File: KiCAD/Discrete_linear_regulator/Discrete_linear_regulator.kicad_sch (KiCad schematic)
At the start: 40 parts, among them J1 Conn_01x06, Q1 PZT2222AT3G, Q10 BC857, Q11 BC857, Q2 BC857, Q3 BC857, Q4 PZT2222AT3G, Q5 PZT2907AT3G, Q8 PZT2907AT3G, U1 LM4562

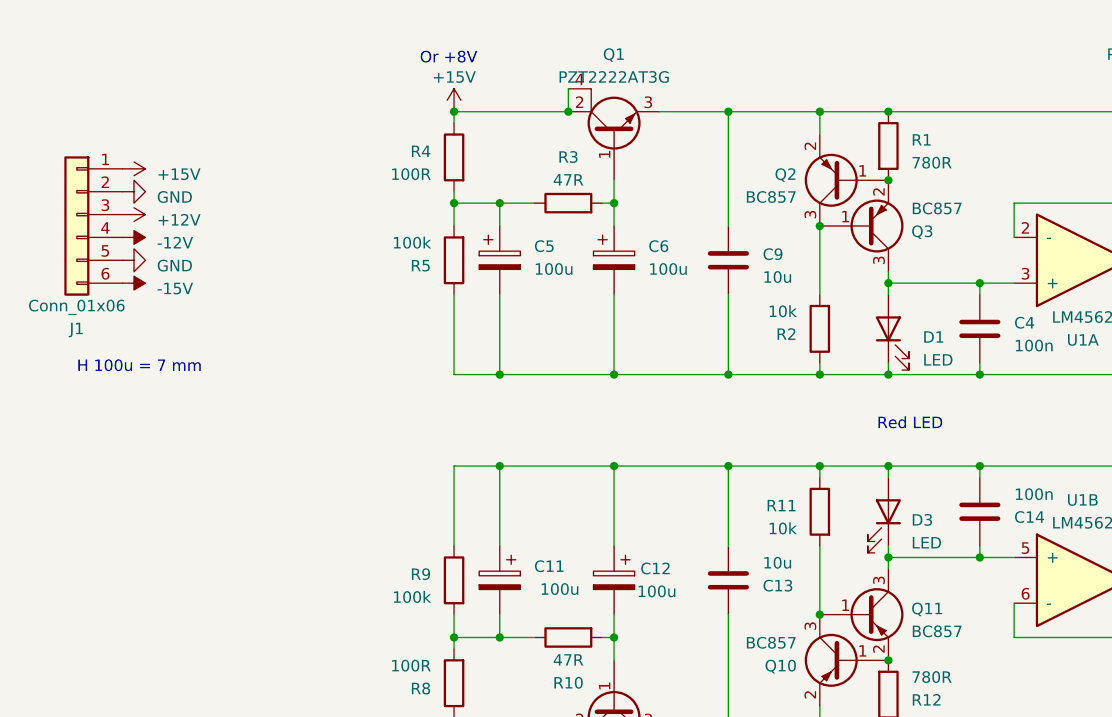
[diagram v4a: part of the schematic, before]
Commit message: linear regulators changes
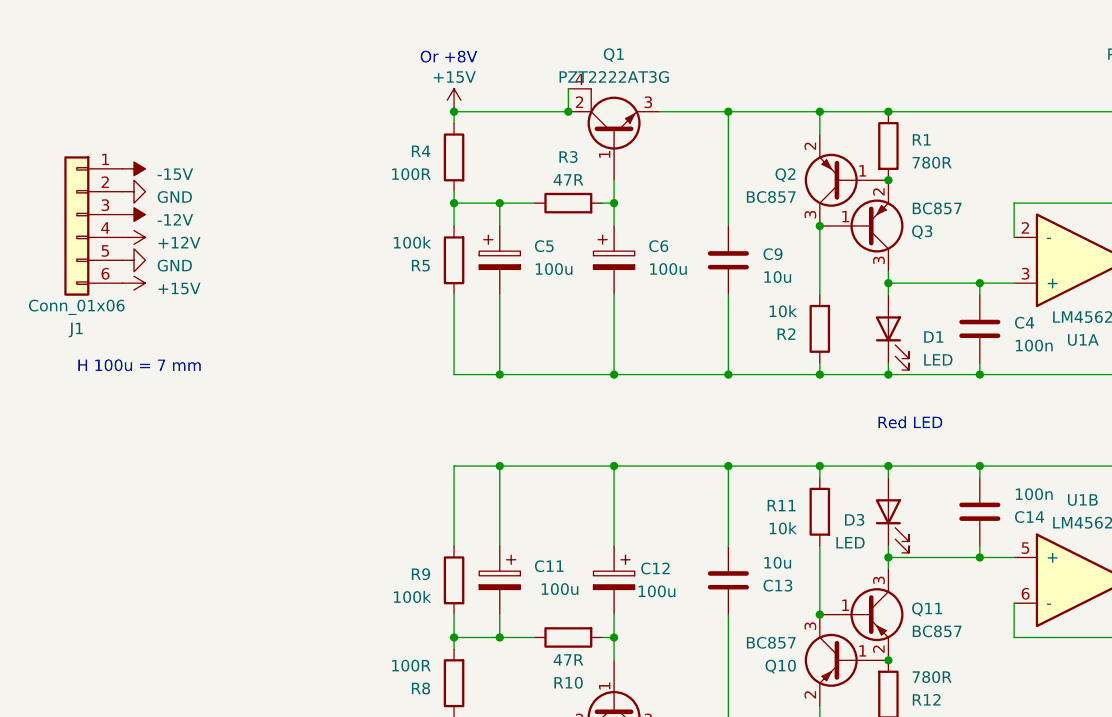
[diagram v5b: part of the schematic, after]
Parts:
- D1, D3: footprint (none) -> LED_SMD:LED_0805_2012Metric
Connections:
- net +12V: now also J1.4 (Pin_4); no longer J1.3 (Pin_3)
- net +15V: now also J1.6 (Pin_6); no longer J1.1 (Pin_1)
- net -12V: now also J1.3 (Pin_3); no longer J1.4 (Pin_4)
- net -15V: now also J1.1 (Pin_1); no longer J1.6 (Pin_6)
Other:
- moved on the sheet: D3
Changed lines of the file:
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@@
       (effects (font (size 1.27 1.27) italic) (justify left) hide)
     )
-    (property "Datasheet" "https://www.onsemi.com/pub/Collateral/BC860-D.pdf" (at 105.41 120.65 0)
+    (property "Datasheet" "" (at 105.41 120.65 0)
       (effects (font (size 1.27 1.27)) (justify left) hide)
     )
@@
     )
   )
+  (symbol (lib_id "power:-15V") (at 25.4 66.04 270) (unit 1)
+    (in_bom yes) (on_board yes) (dnp no) (fields_autoplaced)
+    (property "Reference" "#PWR013" (at 27.94 66.04 0)
+      (effects (font (size 1.27 1.27)) hide)
+    )
+    (property "Value" "-15V" (at 29.21 66.675 90)
+      (effects (font (size 1.27 1.27)) (justify left))
+    )
+    (property "Footprint" "" (at 25.4 66.04 0)
+      (effects (font (size 1.27 1.27)) hide)
+    )
+    (property "Datasheet" "" (at 25.4 66.04 0)
+      (effects (font (size 1.27 1.27)) hide)
+    )
+    (pin "1")
+    (instances
+      (project "Discrete_linear_regulator"
+        (path "/19504711-657f-4df2-b2e9-322b7e64e4f7"
+          (reference "#PWR013") (unit 1)
+        )
+      )
+    )
+  )
+  (symbol (lib_id "power:+15V") (at 25.4 78.74 270) (unit 1)
+    (in_bom yes) (on_board yes) (dnp no) (fields_autoplaced)
+    (property "Reference" "#PWR014" (at 21.59 78.74 0)
+      (effects (font (size 1.27 1.27)) hide)
+    )
+    (property "Value" "+15V" (at 29.21 79.375 90)
+      (effects (font (size 1.27 1.27)) (justify left))
+    )
+    (property "Footprint" "" (at 25.4 78.74 0)
+      (effects (font (size 1.27 1.27)) hide)
+    )
+    (property "Datasheet" "" (at 25.4 78.74 0)
+      (effects (font (size 1.27 1.27)) hide)
+    )
+    (pin "1")
+    (instances
+      (project "Discrete_linear_regulator"
+        (path "/19504711-657f-4df2-b2e9-322b7e64e4f7"
+          (reference "#PWR014") (unit 1)
+        )
+      )
+    )
+  )
   (symbol (lib_id "Audio_DSP:PZT2222AT3G") (at 80.01 60.96 90) (unit 1)
     (in_bom yes) (on_board yes) (dnp no) (fields_autoplaced)
@@
         (path "/19504711-657f-4df2-b2e9-322b7e64e4f7"
           (reference "C11") (unit 1)
-        )
-      )
-    )
-  )
-  (symbol (lib_id "power:+12V") (at 25.4 71.12 270) (unit 1)
-    (in_bom yes) (on_board yes) (dnp no) (fields_autoplaced)
-    (property "Reference" "#PWR09" (at 21.59 71.12 0)
-      (effects (font (size 1.27 1.27)) hide)
-    )
-    (property "Value" "+12V" (at 29.21 71.755 90)
-      (effects (font (size 1.27 1.27)) (justify left))
-    )
-    (property "Footprint" "" (at 25.4 71.12 0)
-      (effects (font (size 1.27 1.27)) hide)
-    )
-    (property "Datasheet" "" (at 25.4 71.12 0)
-      (effects (font (size 1.27 1.27)) hide)
-    )
-    (pin "1")
-    (instances
-      (project "Discrete_linear_regulator"
-        (path "/19504711-657f-4df2-b2e9-322b7e64e4f7"
-          (reference "#PWR09") (unit 1)
         )
       )
@@
       (effects (font (size 1.27 1.27) italic) (justify left) hide)
     )
-    (property "Datasheet" "https://www.onsemi.com/pub/Collateral/BC860-D.pdf" (at 107.95 72.39 0)
+    (property "Datasheet" "" (at 107.95 72.39 0)
       (effects (font (size 1.27 1.27)) (justify left) hide)
     )
@@
     )
   )
-  (symbol (lib_id "Device:LED") (at 110.49 104.14 270) (mirror x) (unit 1)
-    (in_bom yes) (on_board yes) (dnp no) (fields_autoplaced)
-    (property "Reference" "D3" (at 113.03 105.0925 90)
-      (effects (font (size 1.27 1.27)) (justify left))
-    )
-    (property "Value" "LED" (at 113.03 107.6325 90)
-      (effects (font (size 1.27 1.27)) (justify left))
-    )
-    (property "Footprint" "" (at 110.49 104.14 0)
-      (effects (font (size 1.27 1.27)) hide)
-    )
-    (property "Datasheet" "~" (at 110.49 104.14 0)
+  (symbol (lib_id "Device:LED") (at 110.49 104.14 90) (unit 1)
+    (in_bom yes) (on_board yes) (dnp no)
+    (property "Reference" "D3" (at 107.95 105.0925 90)
+      (effects (font (size 1.27 1.27)) (justify left))
+    )
+    (property "Value" "LED" (at 107.95 107.6325 90)
+      (effects (font (size 1.27 1.27)) (justify left))
+    )
+    (property "Footprint" "LED_SMD:LED_0805_2012Metric" (at 110.49 104.14 0)
+      (effects (font (size 1.27 1.27)) hide)
+    )
+    (property "Datasheet" "https://nl.mouser.com/ProductDetail/Broadcom-Avago/HSMH-C170?qs=YDL0qNrpDT6b21G9HrN9ig%3D%3D" (at 110.49 104.14 0)
       (effects (font (size 1.27 1.27)) hide)
     )
@@
       (effects (font (size 1.27 1.27) italic) (justify left) hide)
     )
-    (property "Datasheet" "https://www.onsemi.com/pub/Collateral/BC860-D.pdf" (at 107.95 115.57 0)
+    (property "Datasheet" "" (at 107.95 115.57 0)
       (effects (font (size 1.27 1.27)) (justify left) hide)
     )
@@
         (path "/19504711-657f-4df2-b2e9-322b7e64e4f7"
           (reference "Q11") (unit 1)
-        )
-      )
-    )
-  )
-  (symbol (lib_id "power:-15V") (at 25.4 78.74 270) (unit 1)
-    (in_bom yes) (on_board yes) (dnp no) (fields_autoplaced)
-    (property "Reference" "#PWR08" (at 27.94 78.74 0)
-      (effects (font (size 1.27 1.27)) hide)
-    )
-    (property "Value" "-15V" (at 29.21 79.375 90)
-      (effects (font (size 1.27 1.27)) (justify left))
-    )
-    (property "Footprint" "" (at 25.4 78.74 0)
-      (effects (font (size 1.27 1.27)) hide)
-    )
-    (property "Datasheet" "" (at 25.4 78.74 0)
-      (effects (font (size 1.27 1.27)) hide)
-    )
-    (pin "1")
-    (instances
-      (project "Discrete_linear_regulator"
-        (path "/19504711-657f-4df2-b2e9-322b7e64e4f7"
-          (reference "#PWR08") (unit 1)
         )
       )
@@
     )
   )
-  (symbol (lib_id "power:+15V") (at 25.4 66.04 270) (unit 1)
-    (in_bom yes) (on_board yes) (dnp no) (fields_autoplaced)
-    (property "Reference" "#PWR07" (at 21.59 66.04 0)
-      (effects (font (size 1.27 1.27)) hide)
-    )
-    (property "Value" "+15V" (at 29.21 66.675 90)
-      (effects (font (size 1.27 1.27)) (justify left))
-    )
-    (property "Footprint" "" (at 25.4 66.04 0)
-      (effects (font (size 1.27 1.27)) hide)
-    )
-    (property "Datasheet" "" (at 25.4 66.04 0)
-      (effects (font (size 1.27 1.27)) hide)
-    )
-    (pin "1")
-    (instances
-      (project "Discrete_linear_regulator"
-        (path "/19504711-657f-4df2-b2e9-322b7e64e4f7"
-          (reference "#PWR07") (unit 1)
-        )
-      )
-    )
-  )
   (symbol (lib_id "power:GND") (at 25.4 76.2 90) (unit 1)
     (in_bom yes) (on_board yes) (dnp no) (fields_autoplaced)
@@
     )
   )
+  (symbol (lib_id "power:+12V") (at 25.4 73.66 270) (unit 1)
+    (in_bom yes) (on_board yes) (dnp no) (fields_autoplaced)
+    (property "Reference" "#PWR07" (at 21.59 73.66 0)
+      (effects (font (size 1.27 1.27)) hide)
+    )
+    (property "Value" "+12V" (at 29.21 74.295 90)
+      (effects (font (size 1.27 1.27)) (justify left))
+    )
+    (property "Footprint" "" (at 25.4 73.66 0)
+      (effects (font (size 1.27 1.27)) hide)
+    )
+    (property "Datasheet" "" (at 25.4 73.66 0)
+      (effects (font (size 1.27 1.27)) hide)
+    )
+    (pin "1")
+    (instances
+      (project "Discrete_linear_regulator"
+        (path "/19504711-657f-4df2-b2e9-322b7e64e4f7"
+          (reference "#PWR07") (unit 1)
+        )
+      )
+    )
+  )
   (symbol (lib_id "power:GND") (at 262.89 71.12 90) (unit 1)
     (in_bom yes) (on_board yes) (dnp no) (fields_autoplaced)
@@
     )
   )
+  (symbol (lib_id "power:-12V") (at 25.4 71.12 270) (unit 1)
+    (in_bom yes) (on_board yes) (dnp no) (fields_autoplaced)
+    (property "Reference" "#PWR08" (at 27.94 71.12 0)
+      (effects (font (size 1.27 1.27)) hide)
+    )
+    (property "Value" "-12V" (at 29.21 71.755 90)
+      (effects (font (size 1.27 1.27)) (justify left))
+    )
+    (property "Footprint" "" (at 25.4 71.12 0)
+      (effects (font (size 1.27 1.27)) hide)
+    )
+    (property "Datasheet" "" (at 25.4 71.12 0)
+      (effects (font (size 1.27 1.27)) hide)
+    )
+    (pin "1")
+    (instances
+      (project "Discrete_linear_regulator"
+        (path "/19504711-657f-4df2-b2e9-322b7e64e4f7"
+          (reference "#PWR08") (unit 1)
+        )
+      )
+    )
+  )
   (symbol (lib_id "Device:C_Polarized") (at 158.75 114.3 0) (mirror y) (unit 1)
     (in_bom yes) (on_board yes) (dnp no)
@@
       (effects (font (size 1.27 1.27)) (justify right))
     )
-    (property "Footprint" "" (at 110.49 83.82 0)
-      (effects (font (size 1.27 1.27)) hide)
-    )
-    (property "Datasheet" "~" (at 110.49 83.82 0)
+    (property "Footprint" "LED_SMD:LED_0805_2012Metric" (at 110.49 83.82 0)
+      (effects (font (size 1.27 1.27)) hide)
+    )
+    (property "Datasheet" "https://nl.mouser.com/ProductDetail/Broadcom-Avago/HSMH-C170?qs=YDL0qNrpDT6b21G9HrN9ig%3D%3D" (at 110.49 83.82 0)
       (effects (font (size 1.27 1.27)) hide)
     )
@@
     )
   )
-  (symbol (lib_id "power:-12V") (at 25.4 73.66 270) (unit 1)
-    (in_bom yes) (on_board yes) (dnp no) (fields_autoplaced)
-    (property "Reference" "#PWR010" (at 27.94 73.66 0)
-      (effects (font (size 1.27 1.27)) hide)
-    )
-    (property "Value" "-12V" (at 29.21 74.295 90)
-      (effects (font (size 1.27 1.27)) (justify left))
-    )
-    (property "Footprint" "" (at 25.4 73.66 0)
-      (effects (font (size 1.27 1.27)) hide)
-    )
-    (property "Datasheet" "" (at 25.4 73.66 0)
-      (effects (font (size 1.27 1.27)) hide)
-    )
-    (pin "1")
-    (instances
-      (project "Discrete_linear_regulator"
-        (path "/19504711-657f-4df2-b2e9-322b7e64e4f7"
-          (reference "#PWR010") (unit 1)
-        )
-      )
-    )
-  )
   (symbol (lib_id "Device:R") (at 62.23 111.76 0) (mirror y) (unit 1)
     (in_bom yes) (on_board yes) (dnp no)
@@
       (effects (font (size 1.27 1.27) italic) (justify left) hide)
     )
-    (property "Datasheet" "https://www.onsemi.com/pub/Collateral/BC860-D.pdf" (at 105.41 67.31 0)
+    (property "Datasheet" "" (at 105.41 67.31 0)
       (effects (font (size 1.27 1.27)) (justify left) hide)
     )

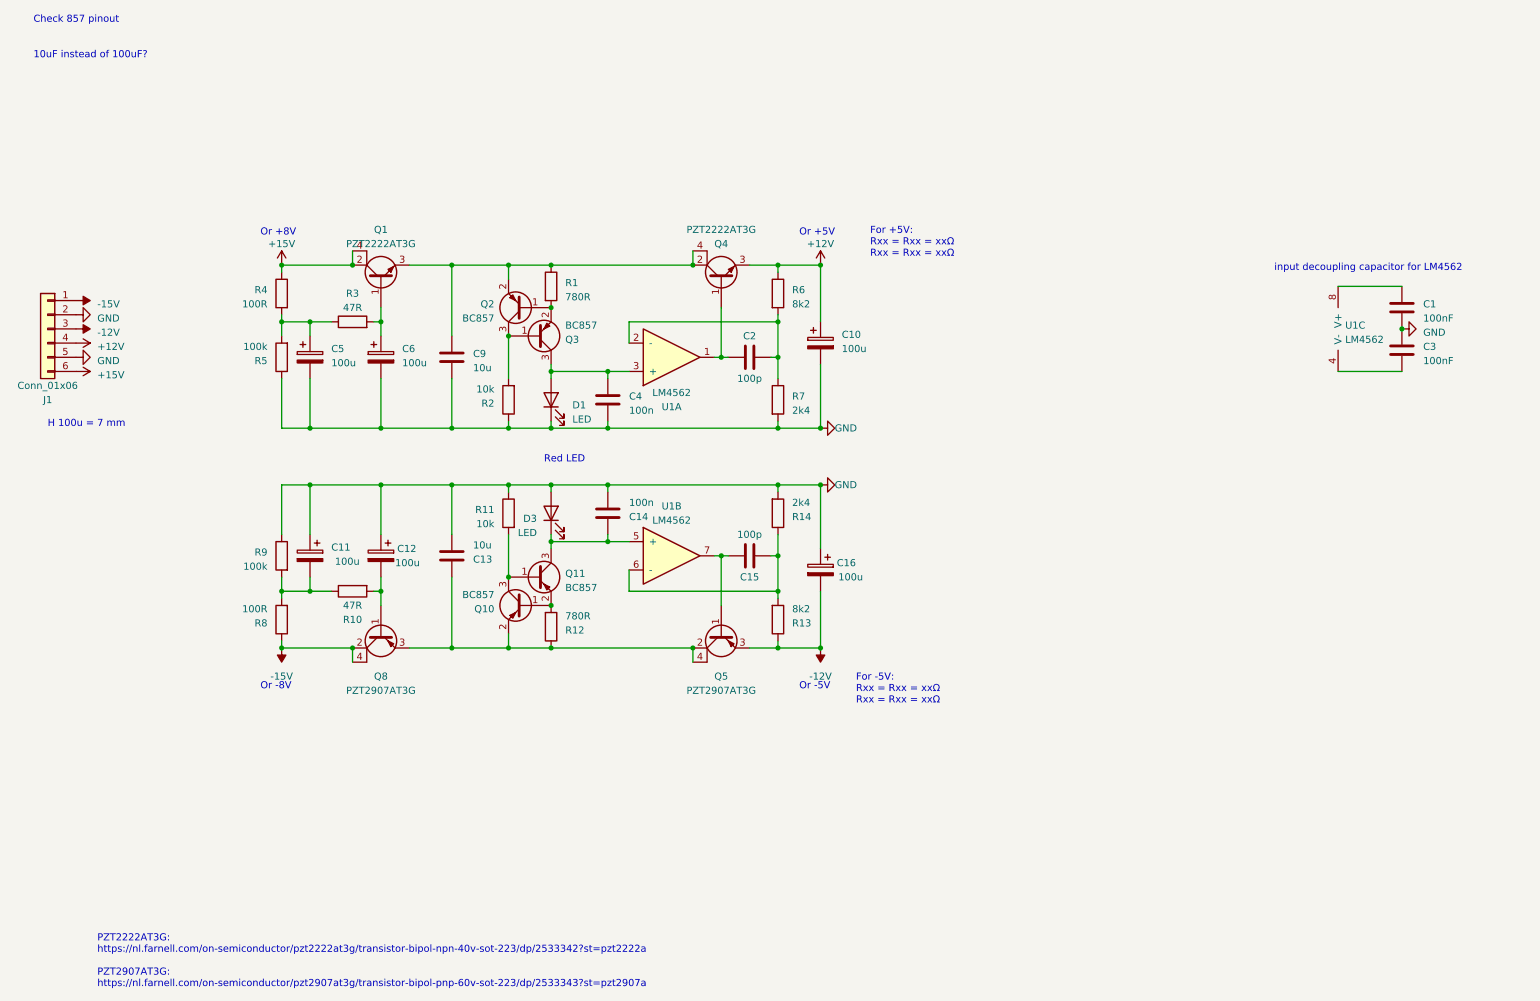
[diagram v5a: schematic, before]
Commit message: update linear regulator pcb
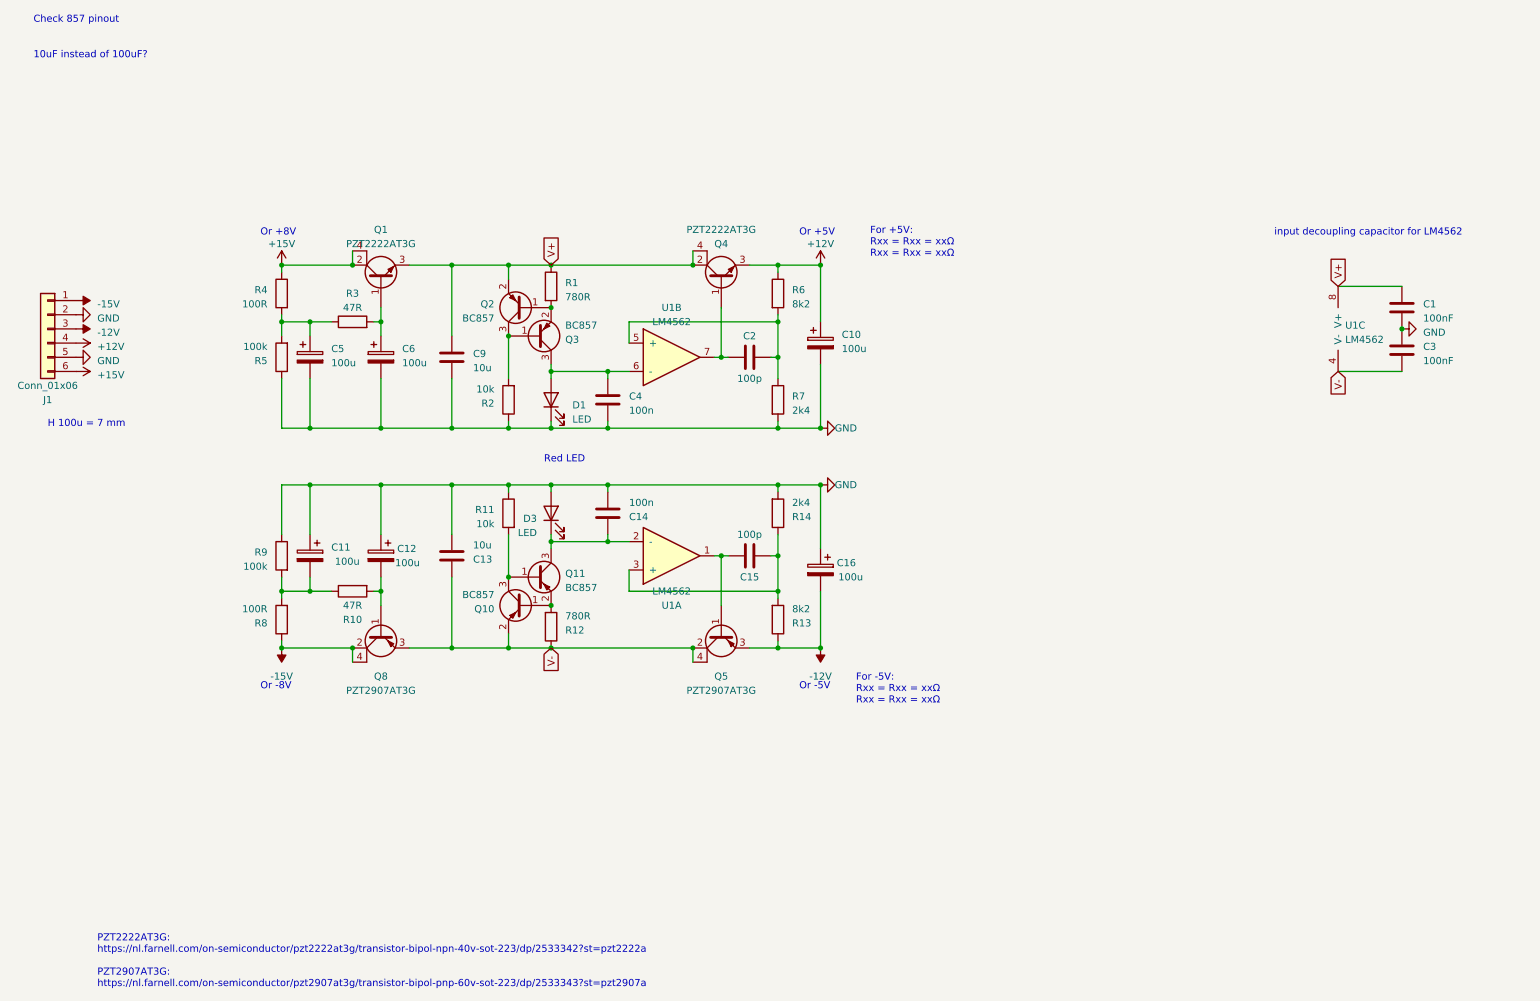
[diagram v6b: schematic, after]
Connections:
- net V-: now reaches C13.1, Q10.2 (E), Q5.2, Q5.4, Q8.3, R12.1
- net V-: now also C3.2, U1.4 (V-)
- net at C2.2, Q4.1: now also U1.7; no longer U1.1
- net at C2.1, R6.2, R7.1: now also U1.5 (+); no longer U1.2 (-)
- net at C4.1, D1.2 (A), Q3.3 (C): now also U1.6 (-); no longer U1.3 (+)
- net V+: now reaches C1.1, U1.8 (V+)
- net V+: now also C9.1, Q1.3, Q2.2 (E), Q4.2, Q4.4, R1.1
- net at C14.1, D3.1 (K), Q11.3 (C): now also U1.2 (-); no longer U1.5 (+)
- net at C15.1, R13.2, R14.1: now also U1.3 (+); no longer U1.6 (-)
- net at C15.2, Q5.1: now also U1.1; no longer U1.7

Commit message: update linear regulators
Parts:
- R13, R6: value 8k2 -> 6K8
- R14, R7: value 2k4 -> 1K2
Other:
- note added: "For +5V: R6 = R13 = 2K7Ω R7 = R14 = 1K5Ω"
- note removed: "For +5V: Rxx = Rxx = xxΩ Rxx = Rxx = xxΩ"
- note removed: "For -5V: Rxx = Rxx = xxΩ Rxx = Rxx = xxΩ"
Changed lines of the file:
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@@
-    (effects (font (size 1.27 1.27)) (justify left bottom))
-  )
-  (text "For -5V:\nRxx = Rxx = xxΩ\nRxx = Rxx = xxΩ" (at 165.1 138.43 0)
     (effects (font (size 1.27 1.27)) (justify left bottom))
   )
@@
     (effects (font (size 1.27 1.27)) (justify left bottom))
   )
-  (text "For +5V:\nRxx = Rxx = xxΩ\nRxx = Rxx = xxΩ" (at 167.64 58.42 0)
+  (text "For +5V:\nR6 = R13 = 2K7Ω\nR7 = R14 = 1K5Ω" (at 177.8 72.39 0)
     (effects (font (size 1.27 1.27)) (justify left bottom))
   )
@@
   (symbol (lib_id "Device:R") (at 151.13 104.14 0) (mirror x) (unit 1)
     (in_bom yes) (on_board yes) (dnp no) (fields_autoplaced)
-    (property "Reference" "R14" (at 153.67 104.775 0)
-      (effects (font (size 1.27 1.27)) (justify left))
-    )
-    (property "Value" "2k4" (at 153.67 102.235 0)
-      (effects (font (size 1.27 1.27)) (justify left))
+    (property "Reference" "R14" (at 148.59 103.505 0)
+      (effects (font (size 1.27 1.27)) (justify right))
+    )
+    (property "Value" "1K2" (at 148.59 106.045 0)
+      (effects (font (size 1.27 1.27)) (justify right))
     )
     (property "Footprint" "Resistor_SMD:R_0402_1005Metric" (at 149.352 104.14 90)
@@
       (effects (font (size 1.27 1.27)) (justify left))
     )
-    (property "Value" "8k2" (at 153.67 121.285 0)
+    (property "Value" "6K8" (at 153.67 121.285 0)
       (effects (font (size 1.27 1.27)) (justify left))
     )
@@
       (effects (font (size 1.27 1.27)) (justify left))
     )
-    (property "Value" "8k2" (at 153.67 66.675 0)
+    (property "Value" "6K8" (at 153.67 66.675 0)
       (effects (font (size 1.27 1.27)) (justify left))
     )
@@
       (effects (font (size 1.27 1.27)) (justify left))
     )
-    (property "Value" "2k4" (at 153.67 85.725 0)
-      (effects (font (size 1.27 1.27)) (justify left))
-    )
+    (property "Value" "1K2" (at 153.67 85.725 0)
+      (effects (font (size 1.27 1.27)) (justify left))
+    )
